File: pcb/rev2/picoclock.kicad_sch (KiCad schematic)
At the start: 67 parts, among them J1 UART, J10 USB, J11 Alt Power, J12 PWM, J13 AUDIO, J2 AUDIO, J3 xx, J4 xx, J5 Micro_SD_Card_Det1, J6 USB_C_Receptacle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

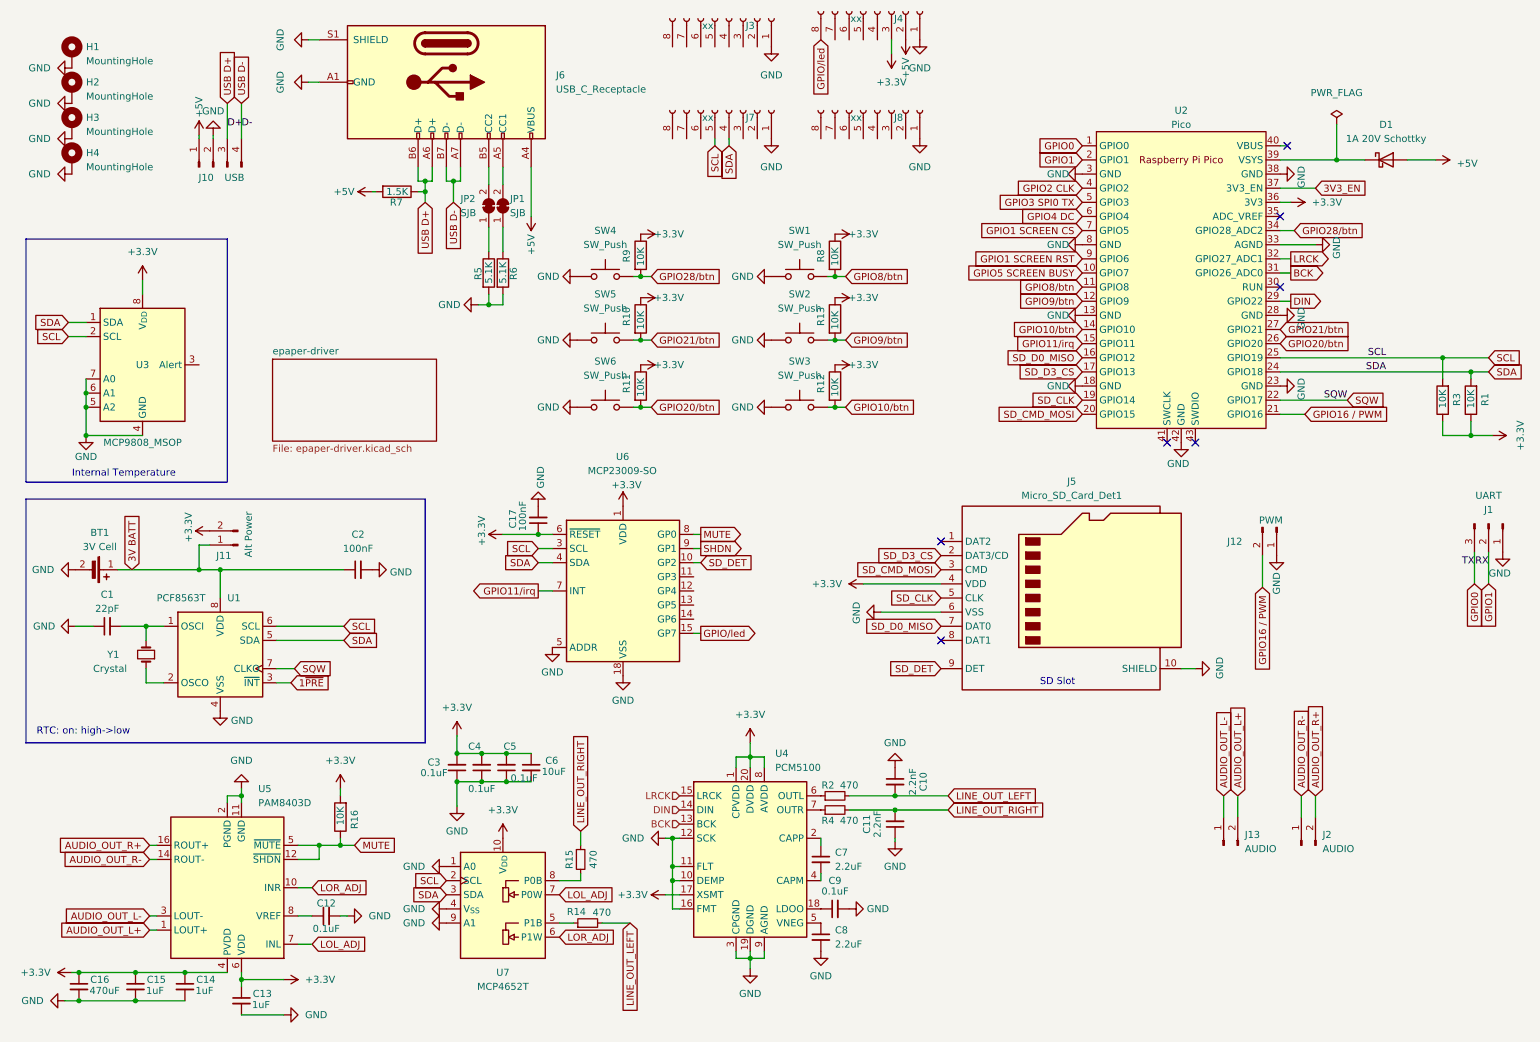
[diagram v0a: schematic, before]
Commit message: [pcb] move rev2 into dedicated folder + start new rev
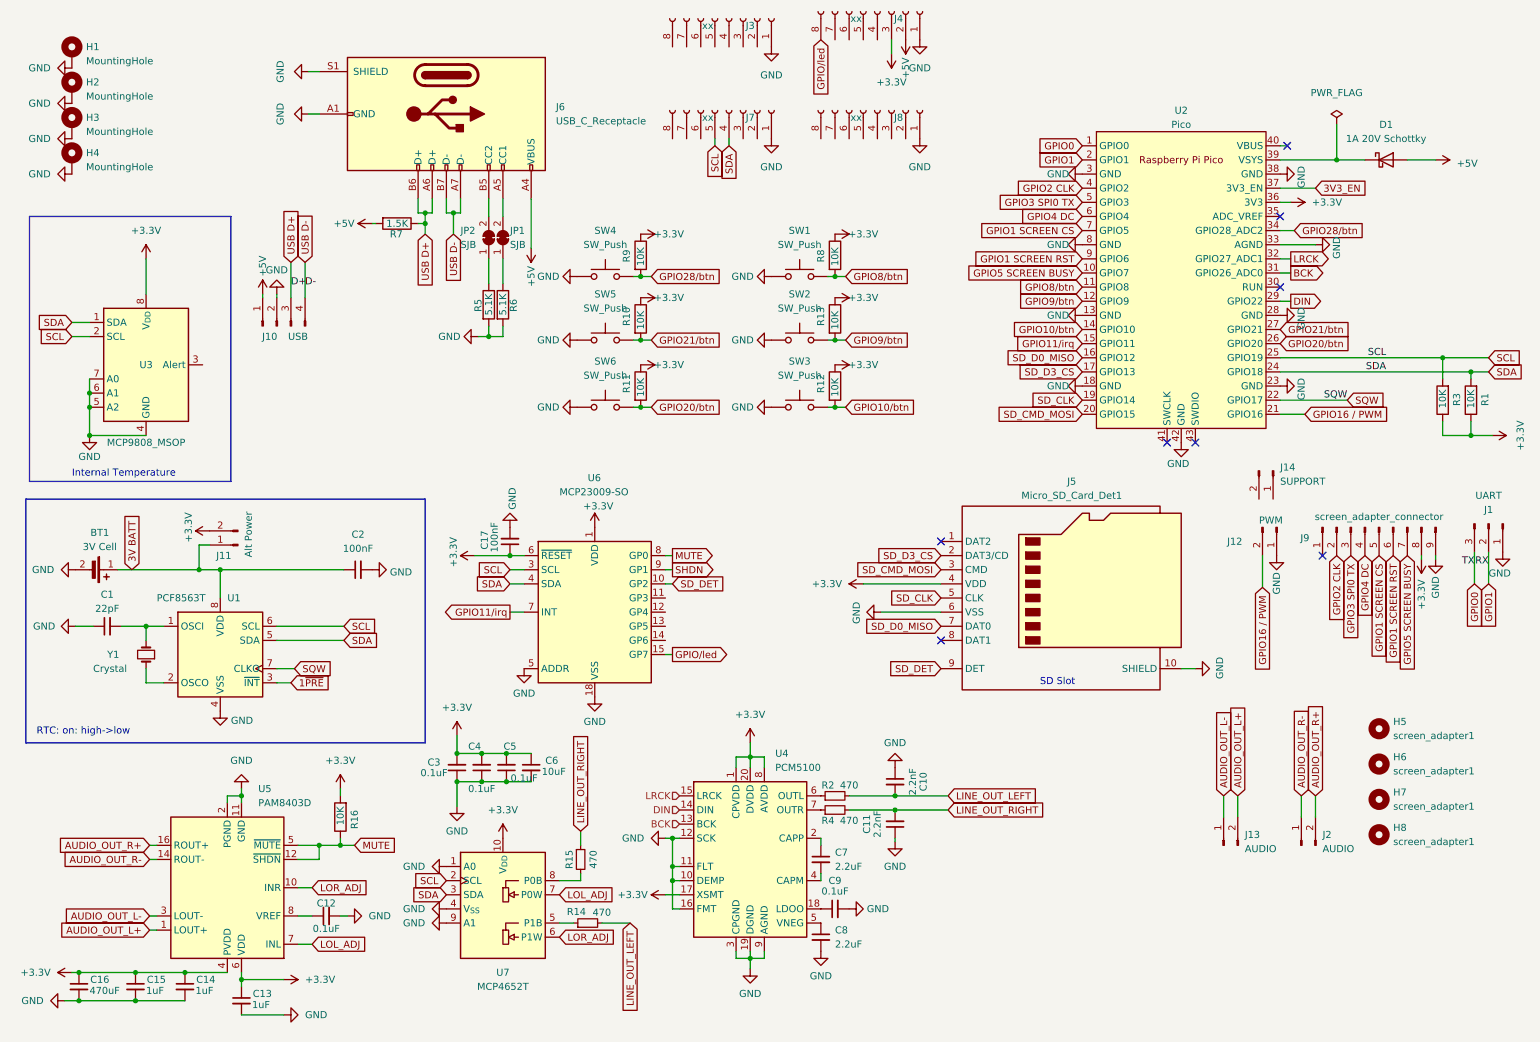
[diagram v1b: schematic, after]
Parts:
- added H5, H6, H7, H8: screen_adapter1, MountingHole:MountingHole_3mm, symbol Mechanical:MountingHole
- added J14: SUPPORT, Connector_PinHeader_2.54mm:PinHeader_1x02_P2.54mm_Vertical, symbol Connector:Conn_01x02_Pin
- added J9: screen_adapter_connector, Connector_PinHeader_2.54mm:PinHeader_1x09_P2.54mm_Vertical, symbol Connector:Conn_01x09_Pin
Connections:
- net +3.3V: now also J9.8 (Pin_8)
- net GND: now also J9.9 (Pin_9)
- net GPIO1 SCREEN CS: now also J9.5 (Pin_5)
- net GPIO1 SCREEN RST: now also J9.6 (Pin_6)
- net GPIO2 CLK: now also J9.2 (Pin_2)
- net GPIO3 SPI0 TX: now also J9.3 (Pin_3)
- net GPIO4 DC: now also J9.4 (Pin_4)
- net GPIO5 SCREEN BUSY: now also J9.7 (Pin_7)
- no-connect marks 7 -> 8
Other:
- removed sheet epaper-driver
- moved on the sheet: C17, J10, J6, JP1, JP2, R5, R6, R7, U3, U6
